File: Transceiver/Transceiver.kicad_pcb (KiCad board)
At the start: 2 copper layers, 100 x 100 mm, 73 parts, among them J1 Conn_02x07, J2 Conn_02x20, J3 Conn_02x20, J4 Conn_02x07, J5 MountingHole, J6 MountingHole, J7 MountingHole, J8 MountingHole, U1 LSM6DS3H

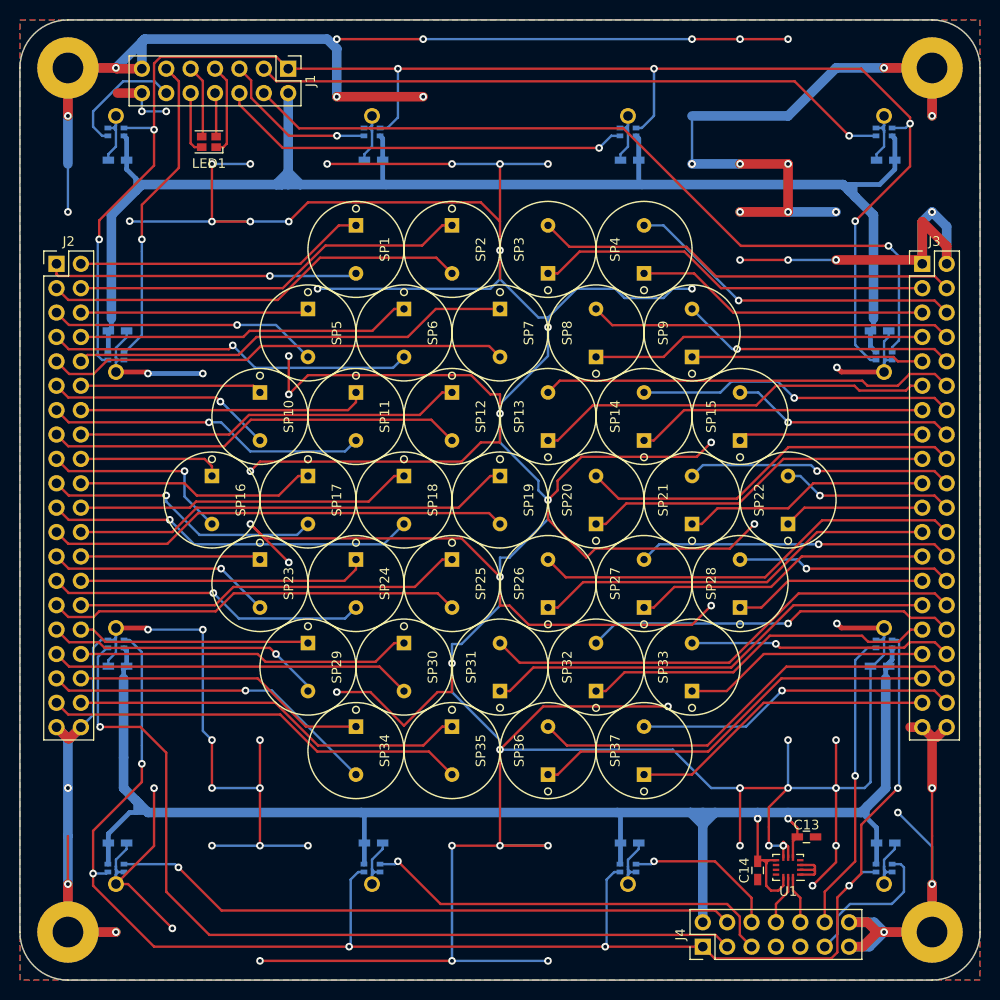
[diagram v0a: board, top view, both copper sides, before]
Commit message: トランシーバ基板修正
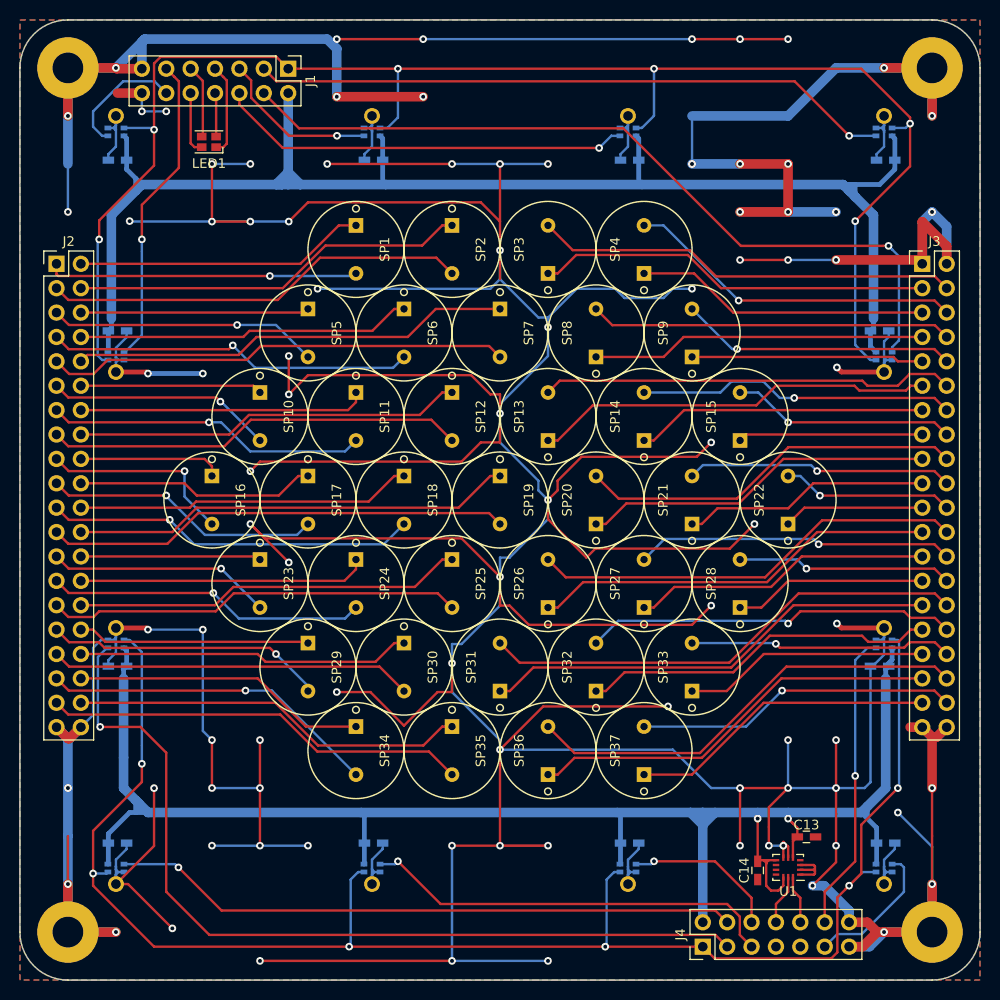
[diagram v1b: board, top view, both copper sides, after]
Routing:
- net GND: track 1106.1 -> 1108.1 mm
- net DATA7: track 15.6 -> 14.5 mm
- net SP36-: track 46.2 -> 46.9 mm
